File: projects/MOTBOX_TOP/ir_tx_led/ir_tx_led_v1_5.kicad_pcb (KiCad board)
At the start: 2 copper layers, 11.9 x 32 mm, 5 parts, among them J1 Conn_01x03

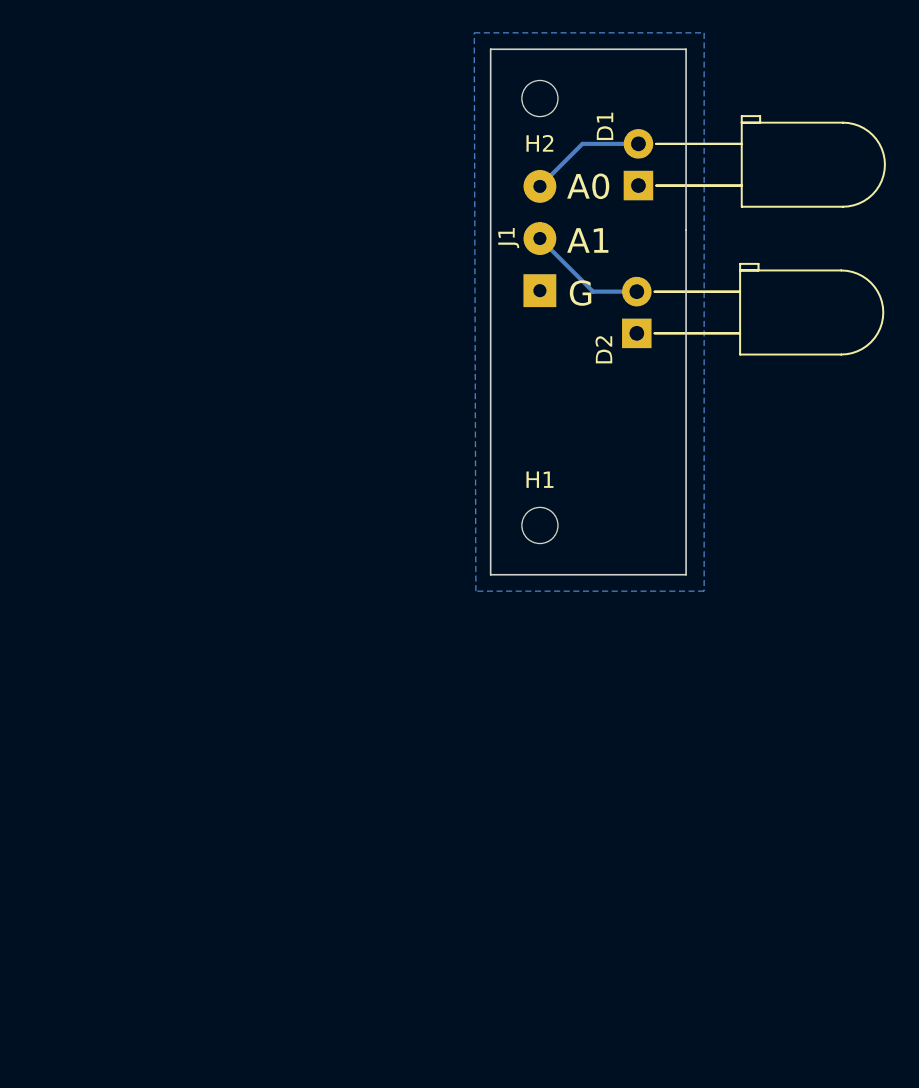
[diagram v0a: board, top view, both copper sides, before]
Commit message: Modified the version 1.5 schematic
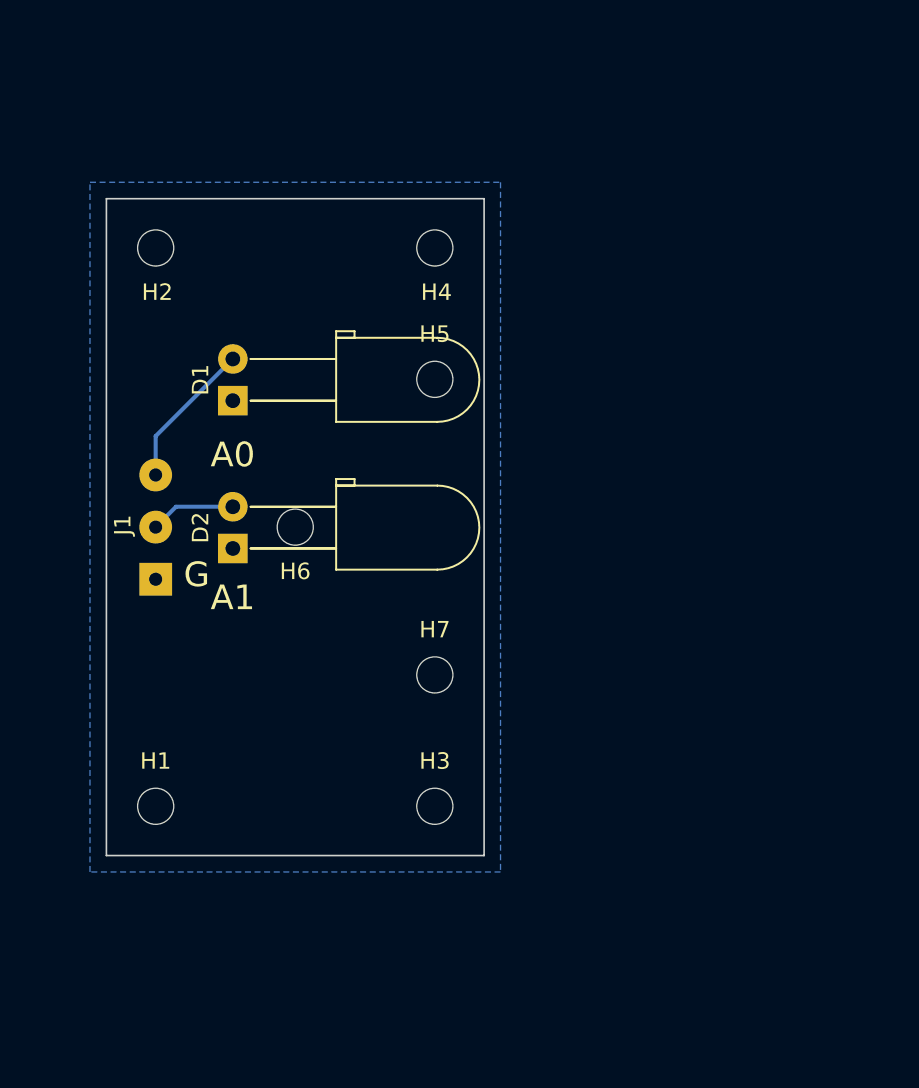
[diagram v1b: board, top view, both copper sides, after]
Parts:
- added H3: MountingHole, MountingHole:MountingHole_2.2mm_M2_ISO7380, F.Cu at (140.8, 98.3)
- added H4: MountingHole, MountingHole:MountingHole_2.2mm_M2_ISO7380, F.Cu at (140.8, 64.3)
- added H5: MountingHole, MountingHole:MountingHole_2.2mm_M2_ISO7380, F.Cu at (140.8, 72.3)
- added H6: MountingHole, MountingHole:MountingHole_2.2mm_M2_ISO7380, F.Cu at (132.3, 81.3)
- added H7: MountingHole, MountingHole:MountingHole_2.2mm_M2_ISO7380, F.Cu at (140.8, 90.3)
- moved J1 29.3 mm to (123.8, 84.5)
- moved H1 29.0 mm to (123.8, 98.3)
- moved D1 28.0 mm to (128.5, 73.6)
- moved D2 27.9 mm to (128.5, 82.6)
- moved H2 25.1 mm to (123.8, 64.3)
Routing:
- net Net-(D2-Pad2): track 7.24 -> 5.21 mm
- net Net-(D1-Pad2): track 7.07 -> 9.01 mm
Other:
- board size 11.9 x 32 mm -> 23 x 40 mm

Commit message: Changes misc
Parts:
- moved H3 11.7 mm to (137.3, 109.5)
- moved H4 11.7 mm to (137.3, 75.5)
- moved H5 11.7 mm to (137.3, 83.5)
- moved H6 11.7 mm to (128.8, 92.5)
- moved H7 11.7 mm to (137.3, 101.5)
- moved H1 11.7 mm to (120.3, 109.5)
- moved H2 11.7 mm to (120.3, 75.5)
- moved D1 11.6 mm to (125.7, 84.8)
- moved D2 11.6 mm to (125.7, 93.8)
- moved J1 11.3 mm to (122.2, 95.7)
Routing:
- net Net-(D2-Pad2): track 5.21 -> 3.96 mm
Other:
- outline, holes or cut-outs redrawn
- board text added: "Cut for the soldering wires added"
- board text added: "IR TX NU V1.5"
- board text removed: "A0"
- board text removed: "A1"

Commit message: Changes for improvments
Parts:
- H1, H2, H3, H4: footprint MountingHole:MountingHole_2.2mm_M2_ISO7380 -> MountingHole:MountingHole_3.2mm_M3_DIN965
- H5, H6, H7: footprint MountingHole:MountingHole_2.2mm_M2_ISO7380 -> MountingHole:MountingHole_2.2mm_M2_DIN965
- moved H5 2.24 mm to (138.3, 81.5)
- moved H7 2.24 mm to (138.3, 103.5)
- moved H1 1.00 mm to (121.3, 109.5)
- moved H2 1.00 mm to (121.3, 75.5)
- moved H3 1.00 mm to (136.3, 109.5)
- moved H4 1.00 mm to (136.3, 75.5)
- moved D1 0.68 mm to (125.2, 85.3)
- moved D2 0.50 mm to (125.2, 93.8)
- moved H6 0.50 mm to (128.3, 92.5)
- moved J1 0.50 mm to (121.7, 95.7)
